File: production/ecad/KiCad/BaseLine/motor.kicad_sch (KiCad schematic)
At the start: 8 parts, among them J5 VibeMotorConnector, U2 DRV8830DGQR

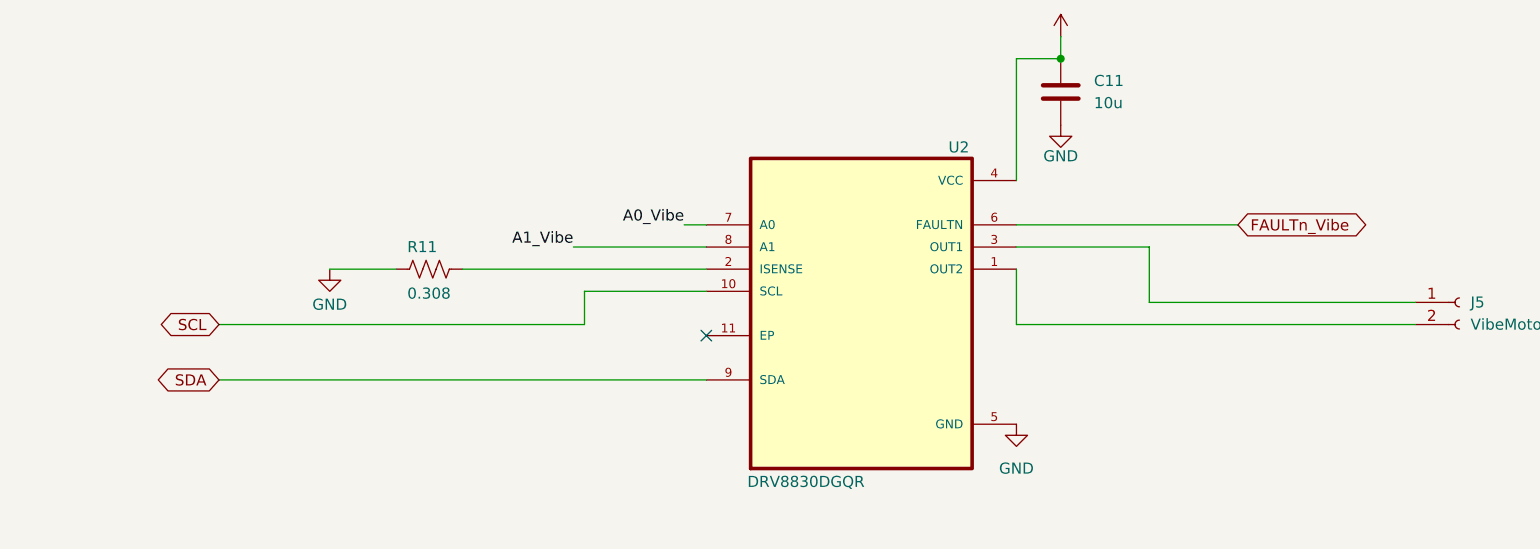
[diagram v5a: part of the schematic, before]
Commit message: MCU connections and matching names
matched the global net names of all the sensor connections with the MCU. Added an IO sheet for the power button
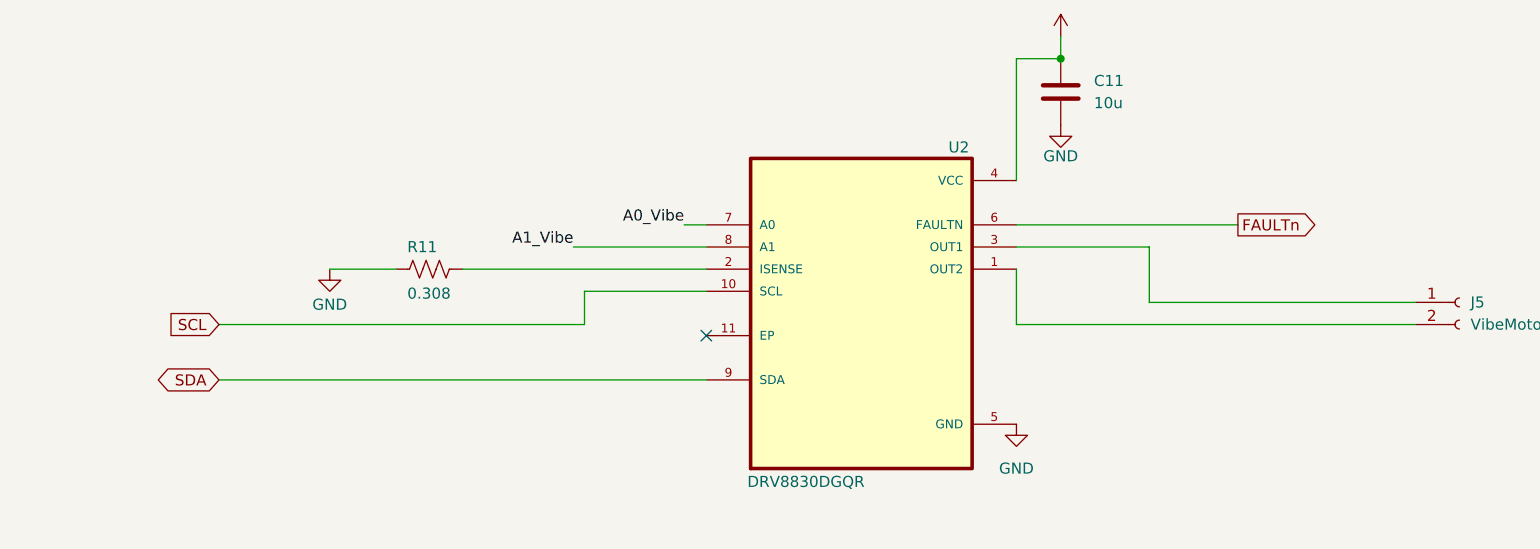
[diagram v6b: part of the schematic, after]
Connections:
- net FAULTn_Vibe renamed FAULTn
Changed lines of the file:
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@@
 		)
 	)
-	(global_label "FAULTn_Vibe"
-		(shape bidirectional)
+	(global_label "FAULTn"
+		(shape output)
 		(at 179.07 91.44 0)
 		(fields_autoplaced yes)
@@
 		)
 		(property "Intersheetrefs" "${INTERSHEET_REFS}"
-			(at 194.7175 91.44 0)
+			(at 188.7076 91.44 0)
 			(effects
 				(font
@@
 	)
 	(global_label "SCL"
-		(shape bidirectional)
+		(shape input)
 		(at 62.23 102.87 180)
 		(fields_autoplaced yes)
@@
 		)
 		(property "Intersheetrefs" "${INTERSHEET_REFS}"
-			(at 54.6259 102.87 0)
+			(at 55.7372 102.87 0)
 			(effects
 				(font

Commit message: Changed annotations
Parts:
- renumbered C11 to C1, J5 to J1, R14 to R1, R15 to R2, R16 to R3, R17 to R4, R11 to R5, U2 to U1
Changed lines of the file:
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@@
 		(dnp no)
 		(fields_autoplaced yes)
-		(property "Reference" "#PWR029"
+		(property "Reference" "#PWR07"
 			(at 158.75 73.66 0)
 			(effects
@@
 			(project "BaseLine"
 				(path "/ba9eda21-3882-41e1-8265-3d8ac781da20/32bcaf69-2ff4-46a9-8a42-fce7269397e2"
-					(reference "#PWR029")
+					(reference "#PWR07")
 					(unit 1)
 				)
@@
 		(on_board yes)
 		(dnp no)
-		(property "Reference" "R15"
+		(property "Reference" "R2"
 			(at 22.606 157.734 90)
 			(effects
@@
 			(project "BaseLine"
 				(path "/ba9eda21-3882-41e1-8265-3d8ac781da20/32bcaf69-2ff4-46a9-8a42-fce7269397e2"
-					(reference "R15")
+					(reference "R2")
 					(unit 1)
 				)
@@
 		(dnp no)
 		(fields_autoplaced yes)
-		(property "Reference" "#PWR033"
+		(property "Reference" "#PWR01"
 			(at 19.05 156.21 0)
 			(effects
@@
 			(project "BaseLine"
 				(path "/ba9eda21-3882-41e1-8265-3d8ac781da20/32bcaf69-2ff4-46a9-8a42-fce7269397e2"
-					(reference "#PWR033")
+					(reference "#PWR01")
 					(unit 1)
 				)
@@
 		(on_board yes)
 		(dnp no)
-		(property "Reference" "#PWR027"
+		(property "Reference" "#PWR05"
 			(at 74.93 102.87 0)
 			(effects
@@
 			(project "BaseLine"
 				(path "/ba9eda21-3882-41e1-8265-3d8ac781da20/32bcaf69-2ff4-46a9-8a42-fce7269397e2"
-					(reference "#PWR027")
+					(reference "#PWR05")
 					(unit 1)
 				)
@@
 		(on_board yes)
 		(dnp no)
-		(property "Reference" "U2"
+		(property "Reference" "U1"
 			(at 147.066 82.55 0)
 			(effects
@@
 			(project "BaseLine"
 				(path "/ba9eda21-3882-41e1-8265-3d8ac781da20/32bcaf69-2ff4-46a9-8a42-fce7269397e2"
-					(reference "U2")
+					(reference "U1")
 					(unit 1)
 				)
@@
 		(on_board yes)
 		(dnp no)
-		(property "Reference" "R11"
+		(property "Reference" "R5"
 			(at 83.82 93.98 90)
 			(effects
@@
 			(project "BaseLine"
 				(path "/ba9eda21-3882-41e1-8265-3d8ac781da20/32bcaf69-2ff4-46a9-8a42-fce7269397e2"
-					(reference "R11")
+					(reference "R5")
 					(unit 1)
 				)
@@
 		(on_board yes)
 		(dnp no)
-		(property "Reference" "R17"
+		(property "Reference" "R4"
 			(at 59.436 158.75 90)
 			(effects
@@
 			(project "BaseLine"
 				(path "/ba9eda21-3882-41e1-8265-3d8ac781da20/32bcaf69-2ff4-46a9-8a42-fce7269397e2"
-					(reference "R17")
+					(reference "R4")
 					(unit 1)
 				)
@@
 		(on_board yes)
 		(dnp no)
-		(property "Reference" "R14"
+		(property "Reference" "R1"
 			(at 22.86 149.86 90)
 			(effects
@@
 			(project "BaseLine"
 				(path "/ba9eda21-3882-41e1-8265-3d8ac781da20/32bcaf69-2ff4-46a9-8a42-fce7269397e2"
-					(reference "R14")
+					(reference "R1")
 					(unit 1)
 				)
@@
 		(dnp no)
 		(fields_autoplaced yes)
-		(property "Reference" "#PWR035"
+		(property "Reference" "#PWR03"
 			(at 55.88 156.21 0)
 			(effects
@@
 			(project "BaseLine"
 				(path "/ba9eda21-3882-41e1-8265-3d8ac781da20/32bcaf69-2ff4-46a9-8a42-fce7269397e2"
-					(reference "#PWR035")
+					(reference "#PWR03")
 					(unit 1)
 				)
@@
 		(dnp no)
 		(fields_autoplaced yes)
-		(property "Reference" "#PWR028"
+		(property "Reference" "#PWR06"
 			(at 153.67 120.65 0)
 			(effects
@@
 			(project "BaseLine"
 				(path "/ba9eda21-3882-41e1-8265-3d8ac781da20/32bcaf69-2ff4-46a9-8a42-fce7269397e2"
-					(reference "#PWR028")
+					(reference "#PWR06")
 					(unit 1)
 				)
@@
 		(dnp no)
 		(fields_autoplaced yes)
-		(property "Reference" "J5"
+		(property "Reference" "J1"
 			(at 205.74 100.3299 0)
 			(effects
@@
 			(project "BaseLine"
 				(path "/ba9eda21-3882-41e1-8265-3d8ac781da20/32bcaf69-2ff4-46a9-8a42-fce7269397e2"
-					(reference "J5")
+					(reference "J1")
 					(unit 1)
 				)
@@
 		(dnp no)
 		(fields_autoplaced yes)
-		(property "Reference" "C11"
+		(property "Reference" "C1"
 			(at 162.56 74.9299 0)
 			(effects
@@
 			(project "BaseLine"
 				(path "/ba9eda21-3882-41e1-8265-3d8ac781da20/32bcaf69-2ff4-46a9-8a42-fce7269397e2"
-					(reference "C11")
+					(reference "C1")
 					(unit 1)
 				)
@@
 		(on_board yes)
 		(dnp no)
-		(property "Reference" "#PWR030"
+		(property "Reference" "#PWR08"
 			(at 158.75 86.36 0)
 			(effects
@@
 			(project "BaseLine"
 				(path "/ba9eda21-3882-41e1-8265-3d8ac781da20/32bcaf69-2ff4-46a9-8a42-fce7269397e2"
-					(reference "#PWR030")
+					(reference "#PWR08")
 					(unit 1)
 				)
@@
 		(dnp no)
 		(fields_autoplaced yes)
-		(property "Reference" "#PWR034"
+		(property "Reference" "#PWR02"
 			(at 19.05 166.37 0)
 			(effects
@@
 			(project "BaseLine"
 				(path "/ba9eda21-3882-41e1-8265-3d8ac781da20/32bcaf69-2ff4-46a9-8a42-fce7269397e2"
-					(reference "#PWR034")
+					(reference "#PWR02")
 					(unit 1)
 				)
@@
 		(on_board yes)
 		(dnp no)
-		(property "Reference" "R16"
+		(property "Reference" "R3"
 			(at 59.69 150.368 90)
 			(effects
@@
 			(project "BaseLine"
 				(path "/ba9eda21-3882-41e1-8265-3d8ac781da20/32bcaf69-2ff4-46a9-8a42-fce7269397e2"
-					(reference "R16")
+					(reference "R3")
 					(unit 1)
 				)
@@
 		(dnp no)
 		(fields_autoplaced yes)
-		(property "Reference" "#PWR036"
+		(property "Reference" "#PWR04"
 			(at 55.88 167.64 0)
 			(effects
@@
 			(project "BaseLine"
 				(path "/ba9eda21-3882-41e1-8265-3d8ac781da20/32bcaf69-2ff4-46a9-8a42-fce7269397e2"
-					(reference "#PWR036")
-					(unit 1)
-				)
+					(reference "#PWR04")
+					(unit 1)
+				)

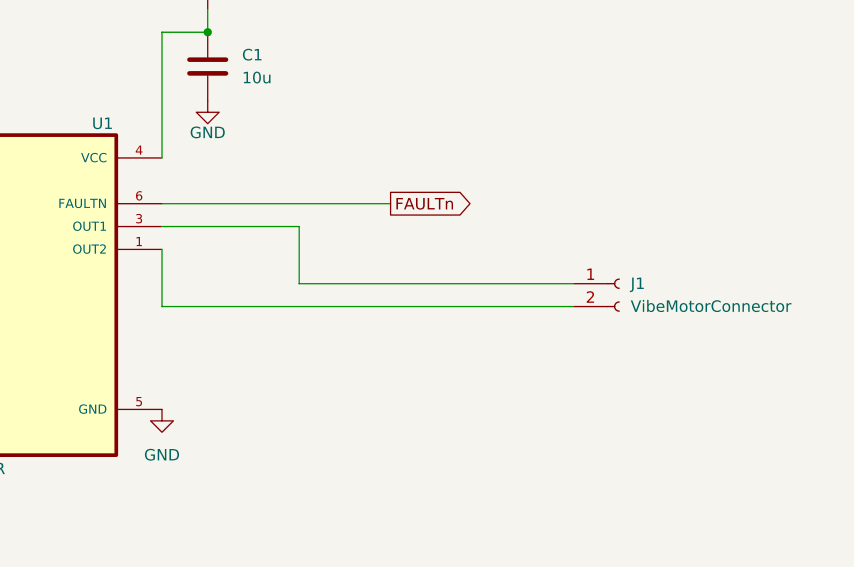
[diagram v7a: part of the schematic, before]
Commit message: Added test points
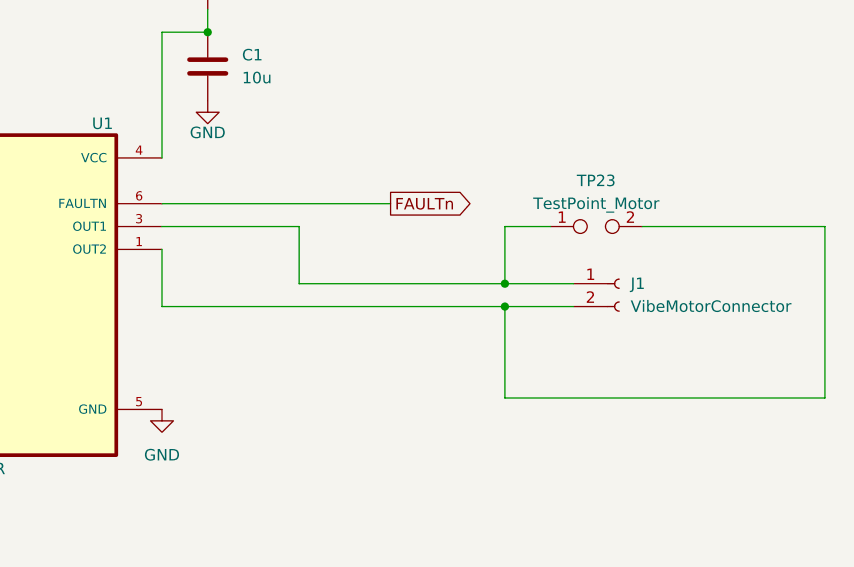
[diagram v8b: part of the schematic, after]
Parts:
- added TP23: TestPoint_Motor, symbol Connector:TestPoint_2Pole
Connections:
- net at J1.2 (Pin_2), U1.1 (OUT2): now also TP23.2
- net at J1.1 (Pin_1), U1.3 (OUT1): now also TP23.1
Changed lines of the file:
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@@
+	)
+	(junction
+		(at 191.77 100.33)
+		(diameter 0)
+		(color 0 0 0 0)
 	)
 	(junction
@@
 		(color 0 0 0 0)
 	)
+	(junction
+		(at 191.77 102.87)
+		(diameter 0)
+		(color 0 0 0 0)
+	)
 	(no_connect
 		(at 118.11 104.14)
@@
 	(wire
 		(pts
-			(xy 168.91 100.33) (xy 199.39 100.33)
+			(xy 191.77 100.33) (xy 199.39 100.33)
+		)
+		(stroke
+			(width 0)
+			(type default)
+		)
+	)
+	(wire
+		(pts
+			(xy 191.77 102.87) (xy 199.39 102.87)
+		)
+		(stroke
+			(width 0)
+			(type default)
+		)
+	)
+	(wire
+		(pts
+			(xy 168.91 100.33) (xy 191.77 100.33)
 		)
 		(stroke
@@
 	(wire
 		(pts
+			(xy 191.77 102.87) (xy 191.77 113.03)
+		)
+		(stroke
+			(width 0)
+			(type default)
+		)
+	)
+	(wire
+		(pts
+			(xy 191.77 93.98) (xy 191.77 100.33)
+		)
+		(stroke
+			(width 0)
+			(type default)
+		)
+	)
+	(wire
+		(pts
 			(xy 29.21 152.4) (xy 26.67 152.4)
 		)
@@
 	(wire
 		(pts
+			(xy 196.85 93.98) (xy 191.77 93.98)
+		)
+		(stroke
+			(width 0)
+			(type default)
+		)
+	)
+	(wire
+		(pts
+			(xy 227.33 113.03) (xy 227.33 93.98)
+		)
+		(stroke
+			(width 0)
+			(type default)
+		)
+	)
+	(wire
+		(pts
+			(xy 227.33 93.98) (xy 207.01 93.98)
+		)
+		(stroke
+			(width 0)
+			(type default)
+		)
+	)
+	(wire
+		(pts
 			(xy 62.23 102.87) (xy 104.14 102.87)
 		)
@@
 	(wire
 		(pts
+			(xy 191.77 113.03) (xy 227.33 113.03)
+		)
+		(stroke
+			(width 0)
+			(type default)
+		)
+	)
+	(wire
+		(pts
 			(xy 69.85 157.48) (xy 77.47 157.48)
 		)
@@
 	(wire
 		(pts
-			(xy 153.67 102.87) (xy 199.39 102.87)
+			(xy 153.67 102.87) (xy 191.77 102.87)
 		)
 		(stroke
@@
 					(unit 1)
 				)
+			)
+		)
+	)
+	(symbol
+		(lib_id "Connector:TestPoint_2Pole")
+		(at 201.93 93.98 0)
+		(unit 1)
+		(exclude_from_sim no)
+		(in_bom yes)
+		(on_board yes)
+		(dnp no)
+		(fields_autoplaced yes)
+		(property "Reference" "TP23"
+			(at 201.93 88.9 0)
+			(effects
+				(font
+					(size 1.27 1.27)
+				)
+			)
+		)
+		(property "Value" "TestPoint_Motor"
+			(at 201.93 91.44 0)
+			(effects
+				(font
+					(size 1.27 1.27)
+				)
+			)
+		)
+		(property "Footprint" ""
+			(at 201.93 93.98 0)
+			(effects
+				(font
+					(size 1.27 1.27)
+				)
+				(hide yes)
+			)
+		)
+		(property "Datasheet" "~"
+			(at 201.93 93.98 0)
+			(effects
+				(font
+					(size 1.27 1.27)
+				)
+				(hide yes)
+			)
+		)
+		(property "Description" "2-polar test point"
+			(at 201.93 93.98 0)
+			(effects
+				(font
+					(size 1.27 1.27)
+				)
+				(hide yes)
+			)
+		)
+		(pin "1"
+		)
+		(pin "2"
+		)
+		(instances
+			(project "BaseLine"
+				(path "/ba9eda21-3882-41e1-8265-3d8ac781da20/32bcaf69-2ff4-46a9-8a42-fce7269397e2"
+					(reference "TP23")
+					(unit 1)
+				)
